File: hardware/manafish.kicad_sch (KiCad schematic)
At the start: 4 parts, among them J6 Battery, J8 USB_C_Receptacle_USB2.0_14P

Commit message: Small fixes
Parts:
- J6: LCSC (none) -> https://www.lcsc.com/product-detail/C431092.html; MPN (none) -> XT30PW-M30.G.Y; Manufacturer (none) -> Amass; Mouser PN (none) -> not stocked; Note (none) -> Not stocked by Mouser: LCSC C431092 or TME XT30PW-M.
- J8: MPN (none) -> USB4105-GF-A; Manufacturer (none) -> GCT; Mouser (none) -> https://www.mouser.com/ProductDetail/640-USB4105-GF-A; Mouser PN (none) -> 640-USB4105-GF-A
- R14, R15: MPN (none) -> RC0402FR-075K1L; Manufacturer (none) -> Yageo; Mouser (none) -> https://www.mouser.com/ProductDetail/603-RC0402FR-075K1L; Mouser PN (none) -> 603-RC0402FR-075K1L
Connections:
- net Power Management/BAT+: now also J6.2 (Pin_2); no longer J6.1 (Pin_1)
- net Power Management/BAT-: now also J6.1 (Pin_1); no longer J6.2 (Pin_2)
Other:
- sheet RP2354A ports: added RP2354_SWCLK, RP2354_SWDIO; removed none
- sheet Rasperry Pi Compute Module 5 ports: added RP2354_SWCLK, RP2354_SWDIO; removed none

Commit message: Update sensor connection, add 3d files
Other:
- sheet I2C Peripherals ports: added I2C0_SCL, I2C0_SDA; removed none
- sheet RP2354A ports: added I2C0_SCL, I2C0_SDA; removed none
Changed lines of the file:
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@@
 	(rectangle
 		(start 15.24 17.78)
-		(end 175.26 114.3)
+		(end 241.3 114.3)
 		(stroke
 			(width 0)
@@
 	(wire
 		(pts
-			(xy 119.38 66.04) (xy 134.62 66.04)
+			(xy 119.38 66.04) (xy 177.8 66.04)
+		)
+		(stroke
+			(width 0)
+			(type default)
+		)
+	)
+	(wire
+		(pts
+			(xy 170.18 88.9) (xy 177.8 88.9)
 		)
 		(stroke
@@
 	(wire
 		(pts
-			(xy 119.38 68.58) (xy 134.62 68.58)
+			(xy 119.38 68.58) (xy 177.8 68.58)
 		)
 		(stroke
@@
 	(wire
 		(pts
+			(xy 170.18 86.36) (xy 177.8 86.36)
+		)
+		(stroke
+			(width 0)
+			(type default)
+		)
+	)
+	(wire
+		(pts
 			(xy 132.08 60.96) (xy 132.08 81.28)
 		)
@@
 	(wire
 		(pts
-			(xy 134.62 60.96) (xy 132.08 60.96)
+			(xy 177.8 60.96) (xy 132.08 60.96)
 		)
 		(stroke
@@
 	)
 	(sheet
-		(at 134.62 58.42)
-		(size 33.02 12.7)
+		(at 177.8 58.42)
+		(size 33.02 50.8)
 		(exclude_from_sim no)
 		(in_bom yes)
@@
 		)
 		(property "Sheetname" "I2C Peripherals"
-			(at 134.62 57.7084 0)
+			(at 177.8 57.7084 0)
 			(show_name no)
 			(do_not_autoplace no)
@@
 		)
 		(property "Sheetfile" "i2c_peripherals.kicad_sch"
-			(at 134.62 71.7046 0)
+			(at 177.8 109.8046 0)
 			(show_name no)
 			(do_not_autoplace no)
@@
 		)
 		(pin "+3.3V" input
-			(at 134.62 60.96 180)
+			(at 177.8 60.96 180)
 			(effects
 				(font
@@
 		)
 		(pin "I2C1_SCL" input
-			(at 134.62 66.04 180)
+			(at 177.8 66.04 180)
 			(effects
 				(font
@@
 		)
 		(pin "I2C1_SDA" bidirectional
-			(at 134.62 68.58 180)
+			(at 177.8 68.58 180)
+			(effects
+				(font
+					(size 1.27 1.27)
+				)
+				(justify left)
+			)
+		)
+		(pin "I2C0_SCL" input
+			(at 177.8 86.36 180)
+			(effects
+				(font
+					(size 1.27 1.27)
+				)
+				(justify left)
+			)
+		)
+		(pin "I2C0_SDA" bidirectional
+			(at 177.8 88.9 180)
 			(effects
 				(font
@@
 	(sheet
 		(at 86.36 22.86)
-		(size 33.02 87.63)
+		(size 33.02 86.36)
 		(exclude_from_sim no)
 		(in_bom yes)
@@
 		)
 		(property "Sheetfile" "cm5.kicad_sch"
-			(at 86.36 111.0746 0)
+			(at 86.36 109.8046 0)
 			(show_name no)
 			(do_not_autoplace no)
@@
 	(sheet
 		(at 134.62 78.74)
-		(size 35.56 31.75)
+		(size 35.56 30.48)
 		(exclude_from_sim no)
 		(in_bom yes)
@@
 		)
 		(property "Sheetfile" "rp2354a.kicad_sch"
-			(at 134.62 111.0746 0)
+			(at 134.62 109.8046 0)
 			(show_name no)
 			(do_not_autoplace no)
@@
 			)
 		)
+		(pin "I2C0_SCL" output
+			(at 170.18 86.36 0)
+			(effects
+				(font
+					(size 1.27 1.27)
+				)
+				(justify right)
+			)
+		)
+		(pin "I2C0_SDA" bidirectional
+			(at 170.18 88.9 0)
+			(effects
+				(font
+					(size 1.27 1.27)
+				)
+				(justify right)
+			)
+		)

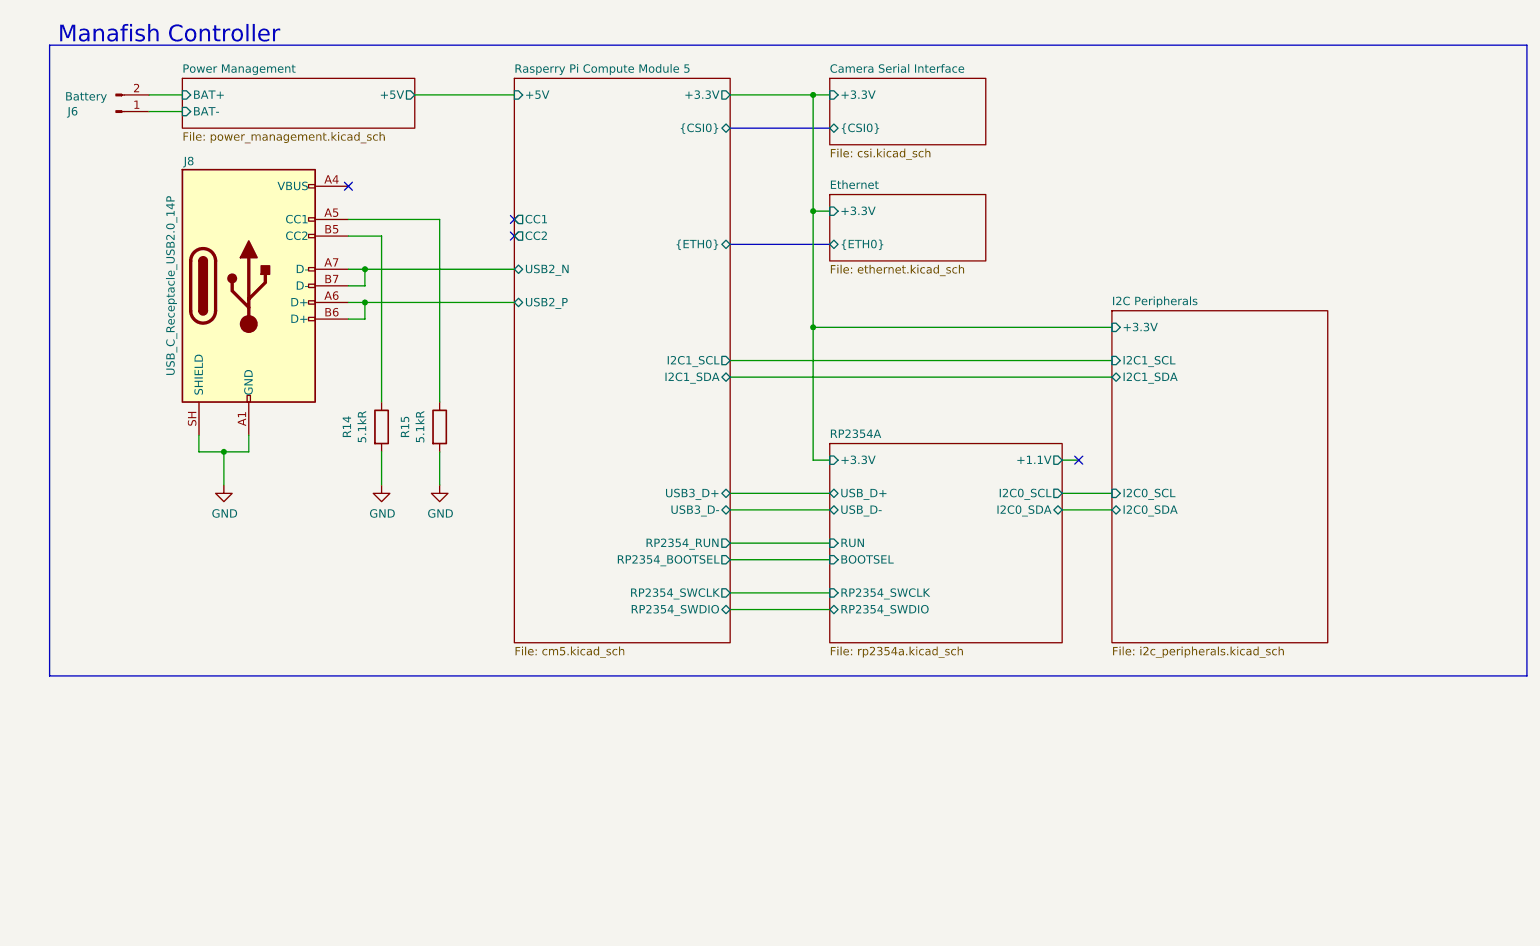
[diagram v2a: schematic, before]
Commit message: Add PoE circuit
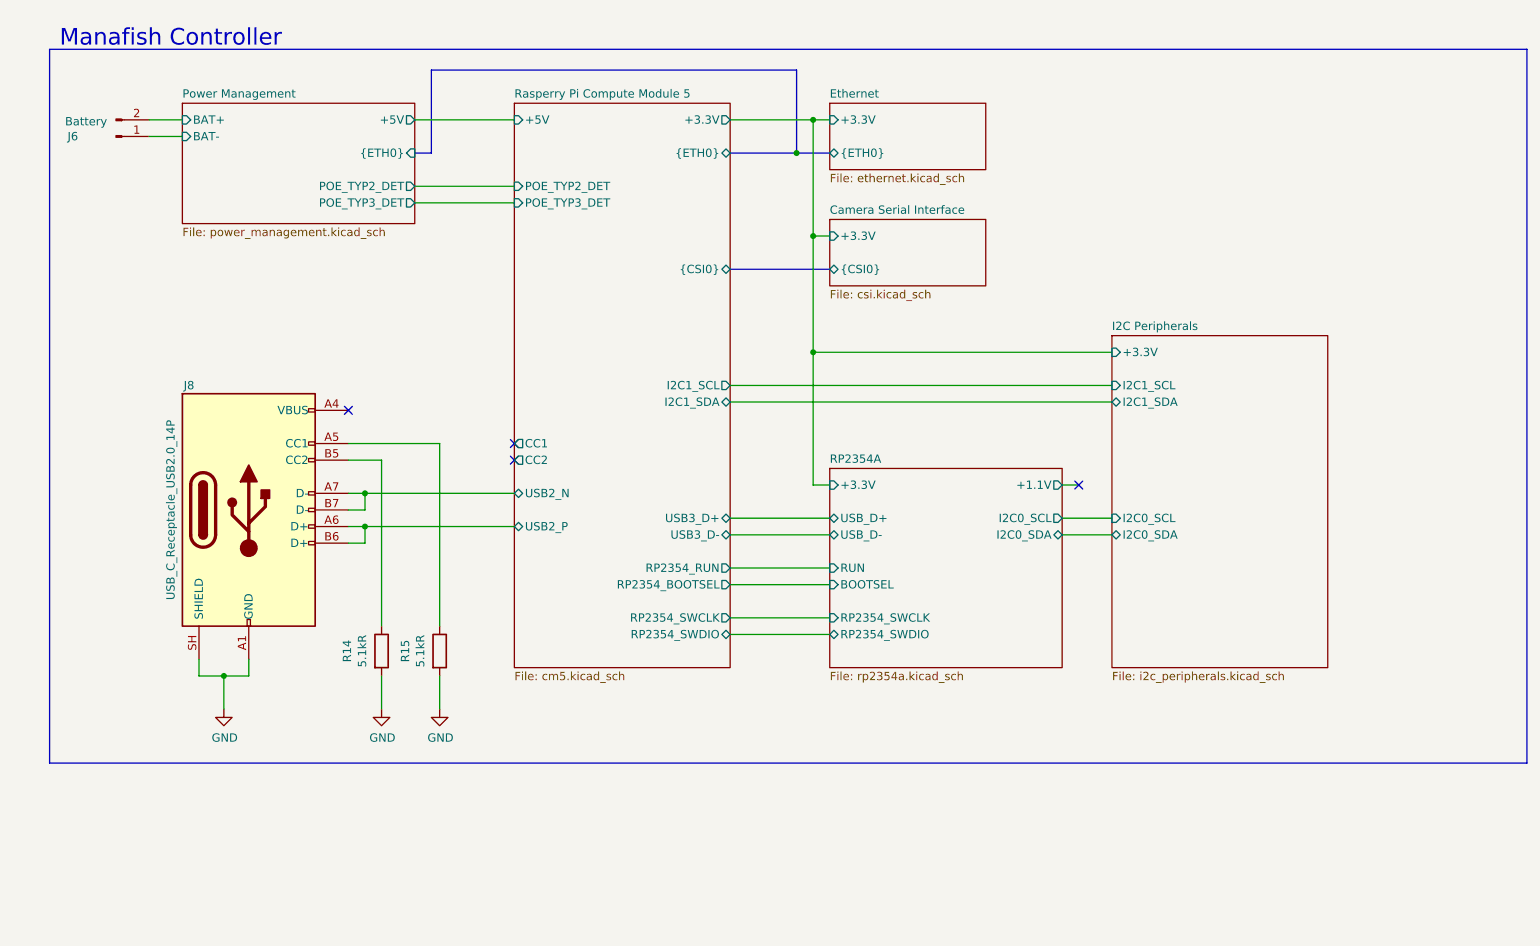
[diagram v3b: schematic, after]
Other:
- sheet Power Management ports: added POE_TYP2_DET, POE_TYP3_DET, {ETH0}; removed none
- sheet Rasperry Pi Compute Module 5 ports: added POE_TYP2_DET, POE_TYP3_DET; removed none
- moved on the sheet: J6, J8, R14, R15

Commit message: Finished power management circuit
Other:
- note added: "TODO: - RJ45 Jack tauschen - Sensor auf SPI - 2ter Kamera-Stecker"
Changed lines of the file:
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@@
+		)
+	)
+	(text "TODO:\n - RJ45 Jack tauschen\n - Sensor auf SPI\n - 2ter Kamera-Stecker"
+		(exclude_from_sim no)
+		(at 20.574 140.716 0)
+		(effects
+			(font
+				(size 2.54 2.54)
+			)
+			(justify left)
 		)
 	)

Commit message: Fix I2C connection
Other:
- sheet Power Management ports: added I2C1_SCL, I2C1_SDA; removed none
- note added: "TODO: - RJ45 Jack tauschen - Sensor auf SPI - 2ter Kamera-Stecker - Drucksensor"
- note removed: "TODO: - RJ45 Jack tauschen - Sensor auf SPI - 2ter Kamera-Stecker"
- moved on the sheet: J6, J8, R14, R15
